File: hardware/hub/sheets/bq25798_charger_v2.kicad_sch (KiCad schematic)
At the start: 39 parts, among them J302 S2B-ZR, Q301 AO3400A, Q302 AO3400A, Q303 AO3400A, Q304 AO3400A, SW3 SW_Push, U8 BQ25798RQMR

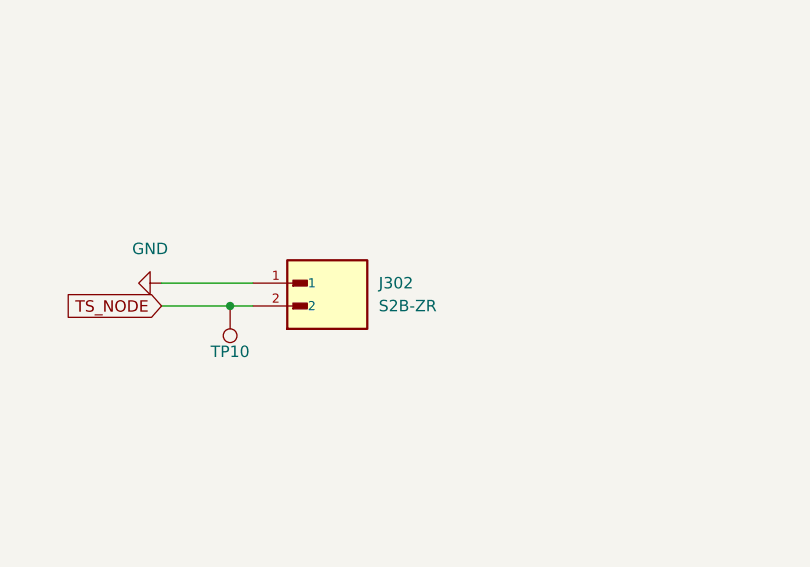
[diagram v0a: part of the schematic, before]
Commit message: Swap thermistor inputs J302/J401 from JST ZH to JST PA
The ZH (S2B-ZR) 1.5 mm housings are impractical to hand-crimp, which
blocks the intended workflow of an end user terminating their own NTC
probe. Move both thermistor inputs to JST PA 2.0 mm side entry
(S02B-PASK-2, LCSC C265094).

Why PA over the alternatives:

- Not PH. J4 (battery input) is already JST PH 2.0 mm; sharing that
  family would let a 4.2 V cell be plugged onto a BQ25798 TS pin.
- Rated -40..+105 C, against -25..+85 C for PH, XH and EH. The connector
  should not be narrower than the range the thermistor qualifies.
- Positive lock. An intermittent TS connection reads as out-of-range and
  suspends charging, so retention matters on a pack-mounted probe.
- 88.9 mm2 courtyard against 105.0 mm2 for XH.

Adds a hand-built footprint for S02B-PASK-2, since none exists in the
stock KiCad libraries. Dimensioned from the JST PA family datasheet
(PC board layout p.3, header dimensions p.9): 2.00 mm pin pitch,
0.7+0.1 mm signal holes, 1.1+0.1 mm NPTH boss holes offset 1.5 mm
outboard of the end pins and 2.1 mm from the pin row, 6.0 x 11.7 mm
body with the pin row 8.2 mm from the mating face.

Docs now specify the Semitec 103AT-11 in place of the 103AT-2. Both are
10 kOhm / B25/85 = 3435 K, but the 103AT-2 ships as a bare bead on 17 mm
solid 42-alloy leads: too short for a crimp barrel, not ductile enough
to form a gas-tight crimp, and with no insulation for the support wings
to grip. The 103AT-11 carries 600 mm of insulated lead. A
solder-to-pigtail fallback is documented for anyone holding 103AT-2
stock, along with a warning that 3D-printer thermistors (100 kOhm,
B ~ 3950) will not work against the 10 kOhm R305/R306 divider.

Also carried here, unrelated to the connector work but coupled to the
same .kicad_pcb: the board's logo footprint moves from
project:Logo-Alternate to project:Logo, with Logo.kicad_mod regenerated.

DRC 0 violations / 0 unconnected; Docusaurus build passes.

Co-Authored-By: Claude Opus 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
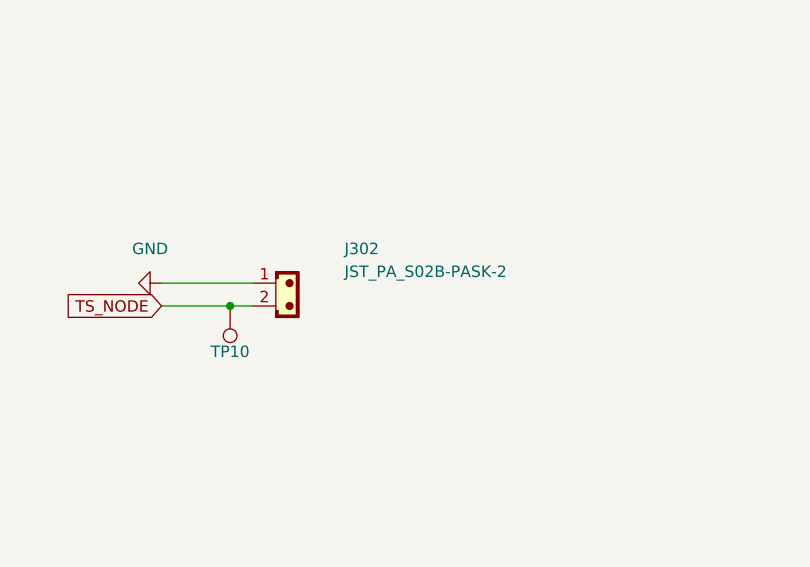
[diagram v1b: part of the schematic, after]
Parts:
- removed J302: S2B-ZR, Snapeda:JST_S2B-ZR_LF__SN_, symbol Snapeda:S2B-ZR_LF__SN_
- added J302: JST_PA_S02B-PASK-2, project:JST_PA_S02B-PASK-2_1x02_P2.00mm_Horizontal, symbol project:JST_02
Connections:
- net GND: now also J302.1
- net TS_NODE: now also J302.2

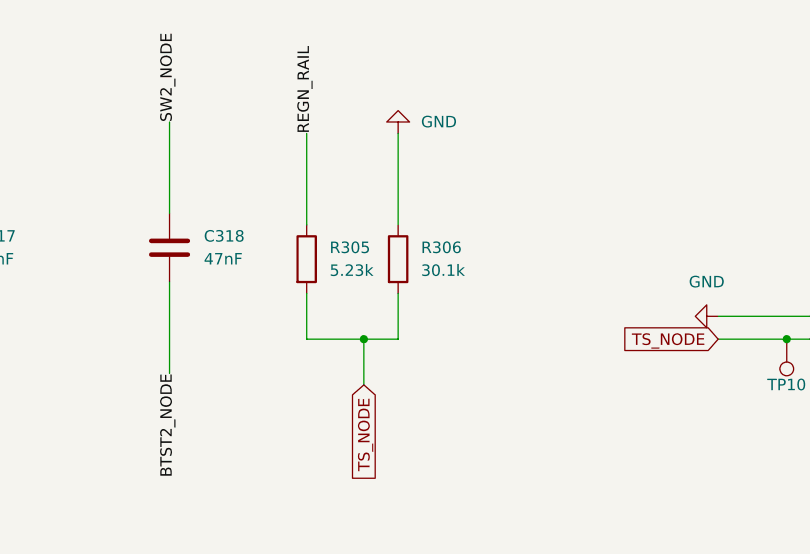
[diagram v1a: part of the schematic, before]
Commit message: Move TS divider R305/R306 to JLCPCB Basic values
R305 5.23k -> 5.1k (C23068 -> C23186) and R306 30.1k -> 30k
(C23000 -> C22984). Both old parts were JLCPCB Extended, carrying
$4.53 each in per-order fees for $0.07 of resistor. The new values
are Basic, and 5.1k is already in the BOM as R5/R6 so R305 adds no
unique part number at all.

Of the 116 Basic/Preferred 0603 resistors in the JLCPCB library,
5.1k/30k is the closest achievable pair to TI's reference network
for a 103AT-type 10k NTC (5.24k/30.31k). The Basic library carries
E24 values only, so the exact E96 values are not available in any
package.

Cost: the JEITA trip points shift about +0.93 C. Against the
documented VT1_RISE of 73.3% of REGN the cold cutoff moves from
roughly +0.97 C to +1.95 C. Both directions are benign for the
LiFePO4 cell this board targets - the cold side errs conservative,
and LiFePO4 tolerates the hot side far better than Li-ion. This is
well inside the VT1 threshold tolerance, which swings the cutoff by
about 3.2 C on its own.

Also updates the values the firmware uses to convert the TS reading
into a temperature. Left stale, ts_resistor_upper/lower would have
reported every cell temperature about 0.85 C low.

Derived constants updated across docs:
  open-circuit divider  85.2% -> 85.5% of REGN
  R306 || 10k NTC @25C  7.506k / 58.9% -> 7.500k / 59.5%

Co-Authored-By: Claude Opus 5 <noreply@anthropic.com>
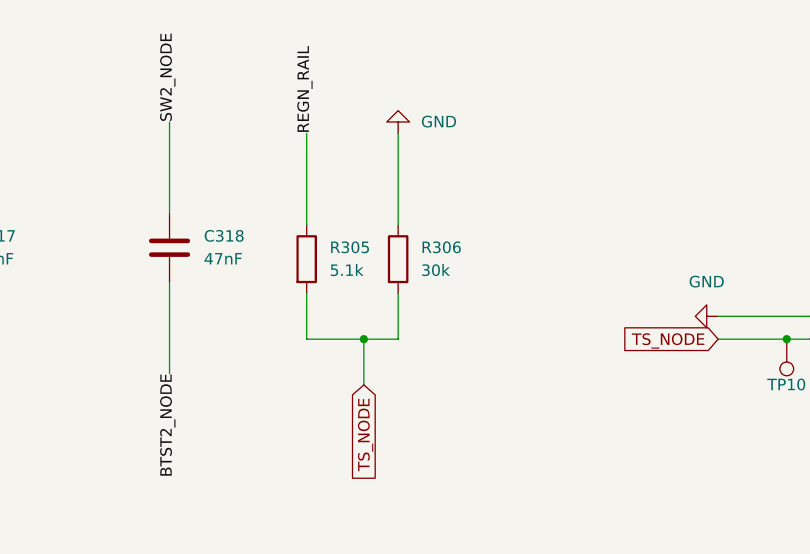
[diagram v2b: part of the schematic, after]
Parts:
- J302: FT Position Offset 0,0 -> 0,1.01600; FT Rotation Offset 0 -> 180
- R305: value 5.23k -> 5.1k; LCSC Part C23068 -> C23186; MPN 0603WAF5231T5E -> 0603WAF5101T5E
- R306: value 30.1k -> 30k; LCSC Part C23000 -> C22984; MPN 0603WAF3012T5E -> 0603WAF3002T5E
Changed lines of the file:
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@@
 			)
 		)
-		(property "FT Rotation Offset" "0"
+		(property "FT Rotation Offset" "180"
 			(at 402.59 154.94 0)
 			(hide yes)
@@
 			)
 		)
-		(property "FT Position Offset" "0,0"
+		(property "FT Position Offset" "0,1.01600"
 			(at 402.59 154.94 0)
 			(hide yes)
@@
 			)
 		)
-		(property "Value" "30.1k"
+		(property "Value" "30k"
 			(at 355.6 148.5899 0)
 			(show_name no)
@@
 			)
 		)
-		(property "Datasheet" "https://datasheet.lcsc.com/datasheet/pdf/0a975aaa49b7c97f38a963127be4a823.pdf?productCode=C23000"
+		(property "Datasheet" "https://jlcpcb.com/partdetail/23711-0603WAF3002T5E/C22984"
 			(at 353.06 147.32 0)
 			(hide yes)
@@
 			)
 		)
-		(property "LCSC Part" "C23000"
+		(property "LCSC Part" "C22984"
 			(at 353.06 147.32 0)
 			(hide yes)
@@
 			)
 		)
-		(property "MPN" "0603WAF3012T5E"
+		(property "MPN" "0603WAF3002T5E"
 			(at 66.04 67.31 0)
 			(hide yes)
@@
 			)
 		)
-		(property "Value" "5.23k"
+		(property "Value" "5.1k"
 			(at 345.44 148.5899 0)
 			(show_name no)
@@
 			)
 		)
-		(property "Datasheet" "https://datasheet.lcsc.com/datasheet/pdf/0a975aaa49b7c97f38a963127be4a823.pdf?productCode=C23068"
+		(property "Datasheet" "https://jlcpcb.com/partdetail/23913-0603WAF5101T5E/C23186"
 			(at 342.9 147.32 0)
 			(hide yes)
@@
 			)
 		)
-		(property "LCSC Part" "C23068"
+		(property "LCSC Part" "C23186"
 			(at 342.9 147.32 0)
 			(hide yes)
@@
 			)
 		)
-		(property "MPN" "0603WAF5231T5E"
+		(property "MPN" "0603WAF5101T5E"
 			(at 86.36 67.31 0)
 			(hide yes)

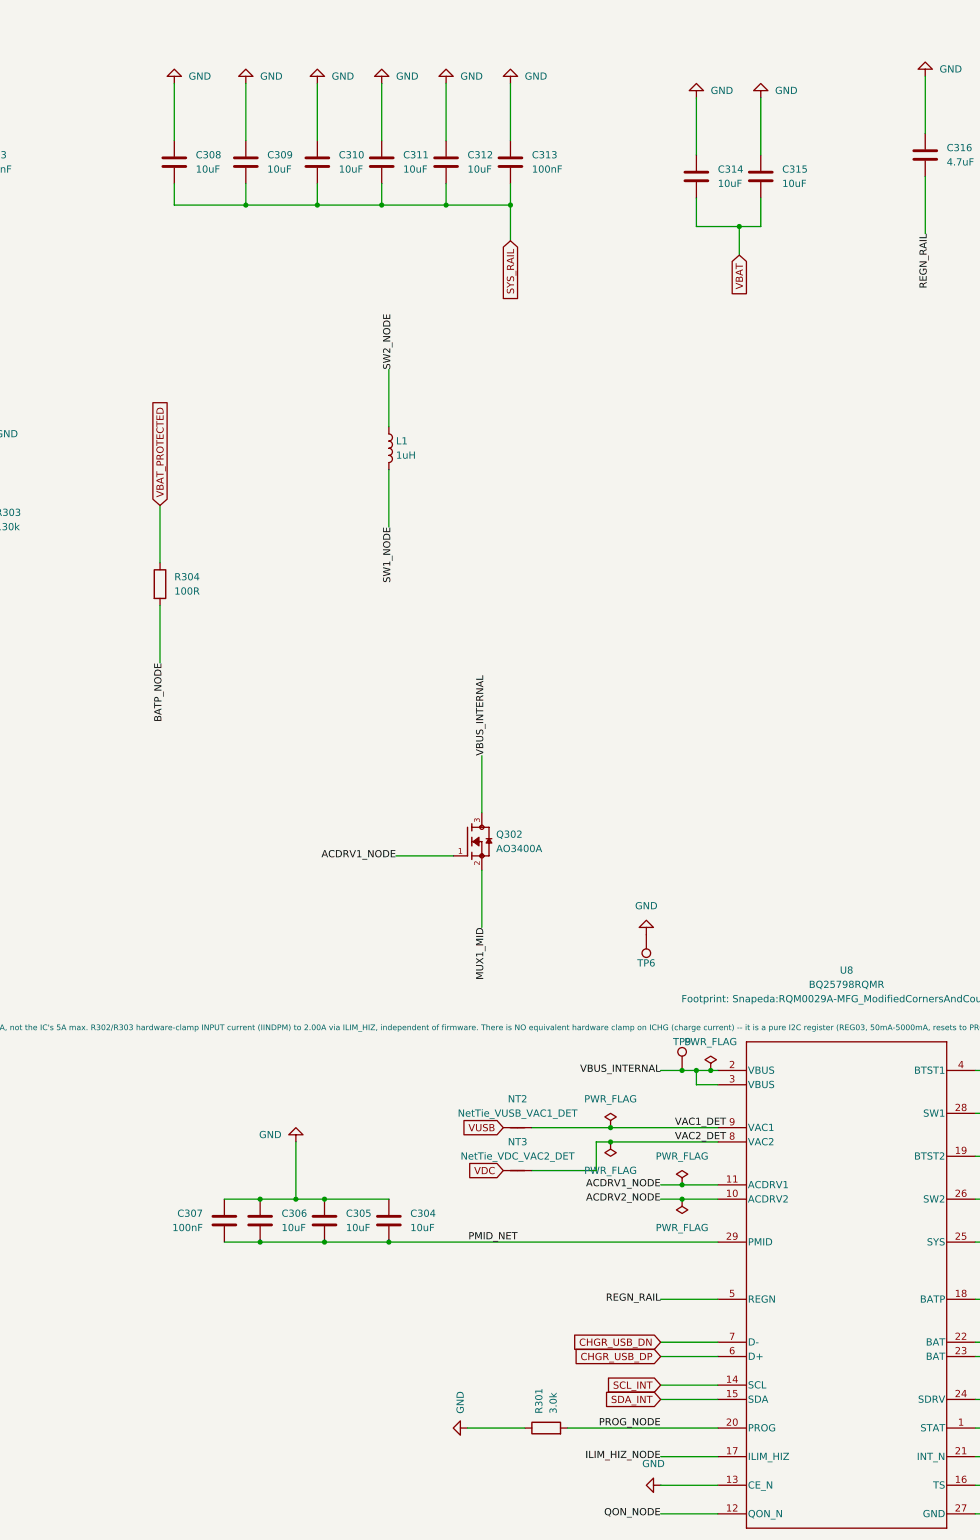
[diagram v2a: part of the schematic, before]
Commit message: Move charger to 750kHz, fix inductor selection, rework USB data tap
Switch the BQ25798 to its 750kHz mode and correct both power inductors,
which were specified from unverifiable data and fitted on a land pattern
JLCPCB flagged as undersized.

Inductors
- R301 3.0k -> 4.7k (C23162, Basic): selects 750kHz/1s per Table 7-1.
- L1 -> FTC404030S2R2MGCA (C39676081), 2.2uH/10.5A/22mOhm. Datasheet
  8.2.2.2 ties inductance to frequency: 750kHz works only with 2.2uH.
- L2 -> FTC252012S1R0MBCD (C22400405), 1uH/6.5A/16mOhm. Not in TI's
  Table 7-2 but beats every listed part; the top entry (Murata
  DFE252012P-1R0M=P2) is 4.3A/42mOhm in the same body.
- Both now use manufacturer-drawn KiCad footprints rather than a generic
  0603/0805 chip land.
- L1 Value corrected from 1uH to 2.2uH; it had been left at the old value
  while the part number changed.

The previous part (C53436345) had no published specs in JLCPCB's library.
The 4A/48mOhm figures carried in the annotations match its FTC201208
siblings, not the part actually fitted.

Firmware constraint on U8: PWM_FREQ (REG0x0F bit 5) is R/W and the PROG
strap only sets its POR default. Firmware must not clear it to 1.5MHz
with a 2.2uH inductor installed.

USB data lines
- R9/R11 10k -> cuttable 0 ohm bridges on a new footprint,
  R_0603_1608Metric_CuttableBridge, excluded from BOM and CPL.
  At 10k the charger's BC1.2 detection could not work: primary detection
  sinks ~100uA and compares against 0.25-0.4V, so 10k contributes 1.0V of
  drop against a 0.6V source.
- JUMP_CHGR_GND2 grounds the charger-side pins after a bridge is cut.
  Cut before grounding: bridging it with the links intact shorts the live
  data lines to ground, and neither DRC nor the ratsnest will catch it.
- D5 now uses USBLC6-4SC6-ES_WIthNetTie, which builds the D+/D- star
  point into the footprint and retires the separate net tie.

Docs
- Correct the false claim that both inductors came from TI's
  recommended-inductor table; the BQ25798 has no such table.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
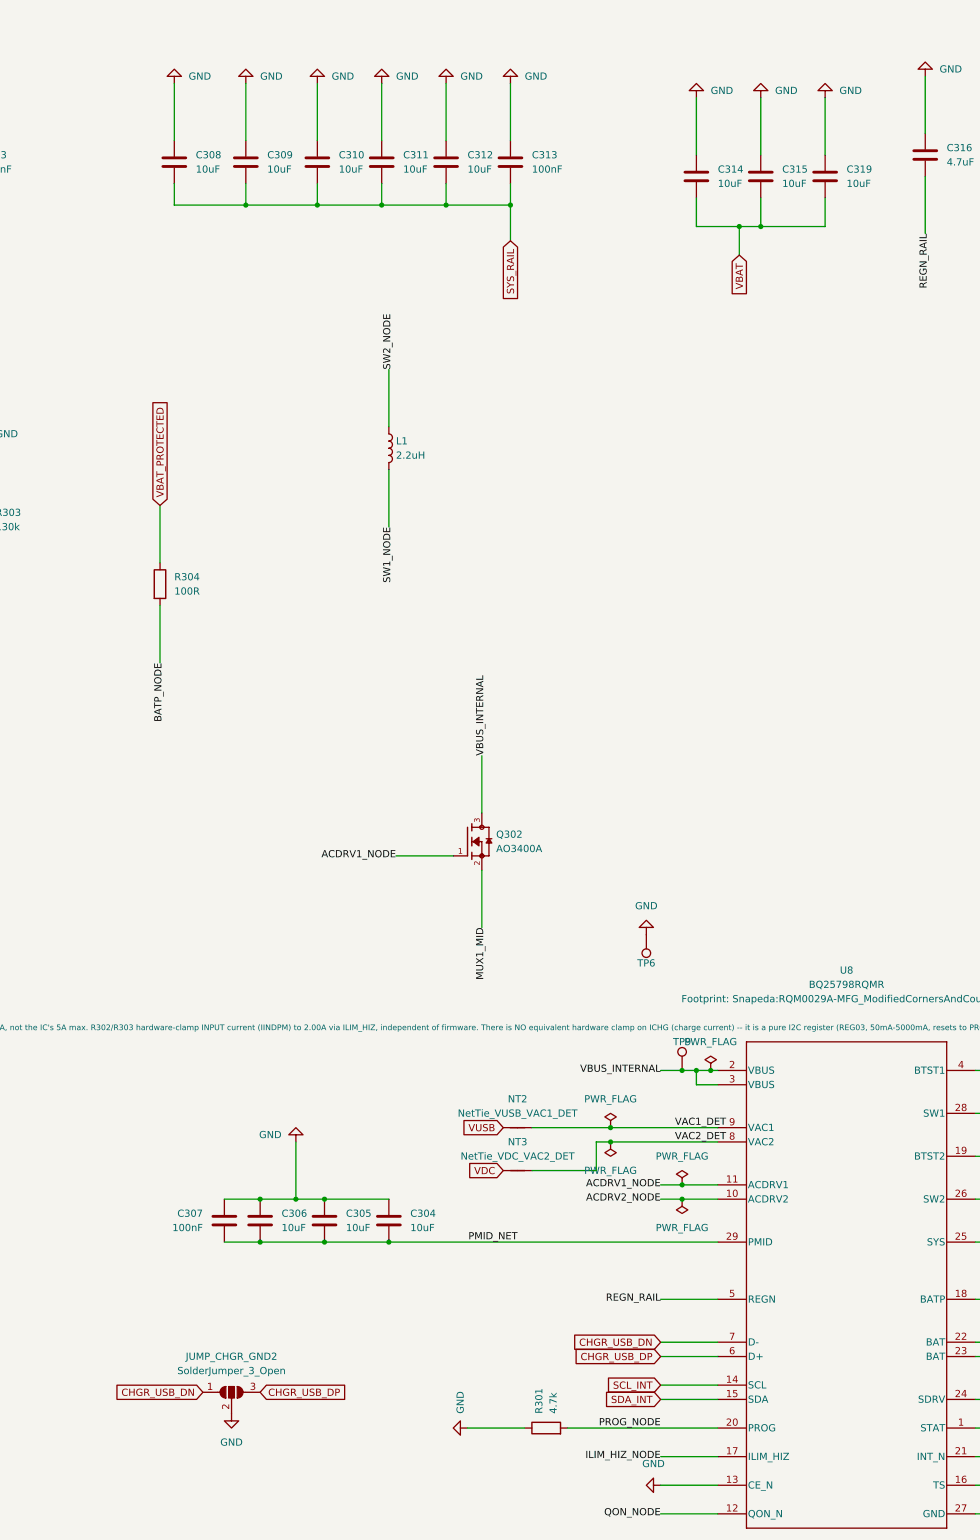
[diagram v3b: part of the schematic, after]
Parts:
- added C319: 10uF, Capacitor_SMD:C_0603_1608Metric, symbol Device:C
- added JUMP_CHGR_GND2: SolderJumper_3_Open, Jumper:SolderJumper-3_P1.3mm_Open_RoundedPad1.0x1.5mm_NumberLabels, symbol Jumper:SolderJumper_3_Open
- C314: Usage Battery input (BAT) decoupling -- bulk cap 1 of 2 for this 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 -> Battery input (BAT) decoupling -- bulk cap 1 of 3 for this 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
- C315: Usage Battery input (BAT) decoupling -- bulk cap 2 of 2 for this 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 -> Battery input (BAT) decoupling -- bulk cap 2 of 3 for this 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
- L1: value 1uH -> 2.2uH; footprint Inductor_SMD:L_0805_2012Metric -> Inductor_SMD:L_Changjiang_FTC404030S; LCSC Part C53436345 -> C39676081; MPN FTC201212S1R0MBCA -> FTC404030S2R2MGCA; Supplier Part Site (none) -> https://jlcpcb.com/partdetail/41398082-FTC404030S2R2MGCA/C3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
- R301: value 3.0k -> 4.7k; LCSC Part C4211 -> C23162; MPN 0603WAF3001T5E -> 0603WAF4701T5E; Usage Sets the POR default cell count (1S) and switching frequency (1.5MHz) via the PROG pin's resistor-to-REGN ratio (datasheet Table 7-1). -> Sets the POR default cell count (1S) and switching frequency (750kHz) via the PROG pin's resistor-to-REGN ratio (datasheet Table 7-1).
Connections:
- net CHGR_USB_DN: now also JUMP_CHGR_GND2.1 (A)
- net CHGR_USB_DP: now also JUMP_CHGR_GND2.3 (B)
- net GND: now also C319.1, JUMP_CHGR_GND2.2 (C)
- net VBAT: now also C319.2

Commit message: Remove TPS631000 output cap C29, regenerate docs-site assets
C29 (1nF) sat on the PCB between U4 and C14, pushing the 47µF output
capacitor - the one the datasheet's Section 7.4.1 layout guidance actually
asks to be closest to VOUT/PGND - further from the IC. Section 7.2.2.3
recommends a single 47µF output cap with no upper limit; C29 was never a
datasheet requirement, so it's gone and C14 can sit where it belongs.

docs/hub/modules/tps631000-regulator.md updated to match (single output
cap). Also corrects an earlier mix-up in tps22918-load-switch.md: C18
(100nF) is TPS22918's VOUT decoupling cap, not a TPS631000 part - it
never belonged in the TPS631000 doc's capacitor table.

Also includes minor trace cleanup on the charger and I2C buffer sheets
(comment visibility, a clarifying note on VCC_2), plus regenerated
website assets (board renders, schematic PDF, interactive BOM, pinout
draft) via tools/generate-docs-assets.sh to reflect the current layout.

Co-Authored-By: Claude Sonnet 5 <noreply@anthropic.com>
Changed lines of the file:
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@@
 		(property "Firmware Constraint" "PCB copper for PMID/SYS/SW1/SW2/BAT (Power_2A net class) is sized for 2A, not the IC's 5A max. R302/R303 hardware-clamp INPUT current (IINDPM) to 2.00A via ILIM_HIZ, independent of firmware. There is NO equivalent hardware clamp on ICHG (charge current) -- it is a pure I2C register (REG03, 50mA-5000mA, resets to PROG-resistor default of 1A on POR/watchdog/REG_RST). Firmware MUST NOT set ICHG above 2000mA (2A); doing so can drive charge-side copper beyond its rated current, since in buck mode (VBUS greater than VBAT) charge current can exceed input current."
 			(at 262.89 300.99 0)
+			(hide yes)
 			(show_name no)
 			(do_not_autoplace no)
